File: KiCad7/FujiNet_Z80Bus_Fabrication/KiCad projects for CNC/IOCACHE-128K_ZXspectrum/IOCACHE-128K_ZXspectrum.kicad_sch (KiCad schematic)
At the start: 4 parts, among them IC4 74HC590N

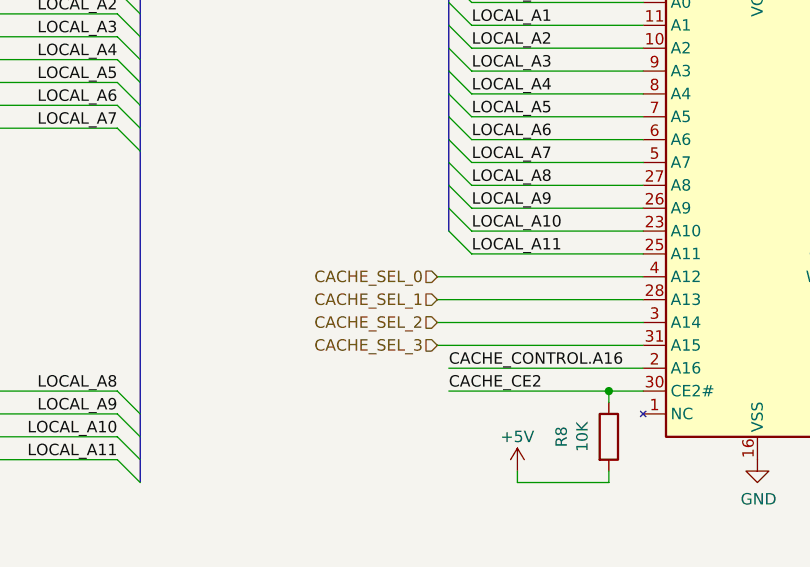
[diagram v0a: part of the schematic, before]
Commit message: KICAD IOCACHE fixed
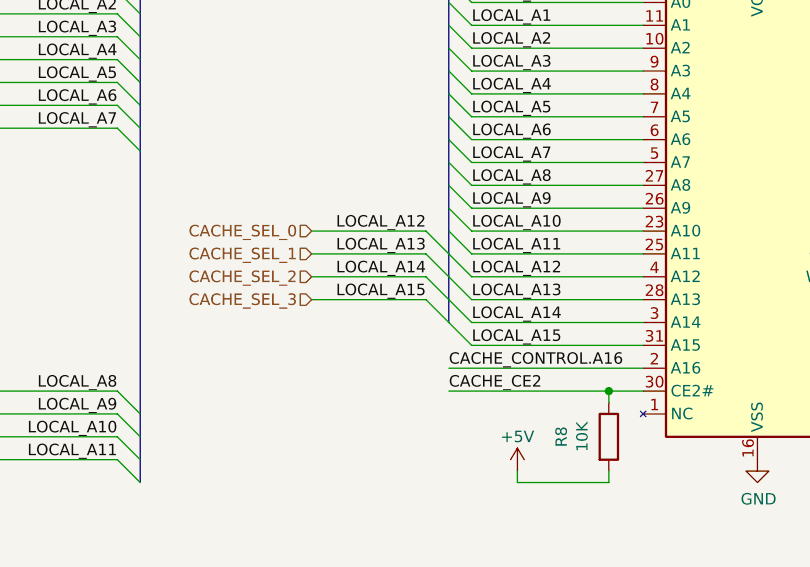
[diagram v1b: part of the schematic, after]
